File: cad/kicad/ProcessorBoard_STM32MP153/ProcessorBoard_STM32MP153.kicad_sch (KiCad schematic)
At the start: 4 parts

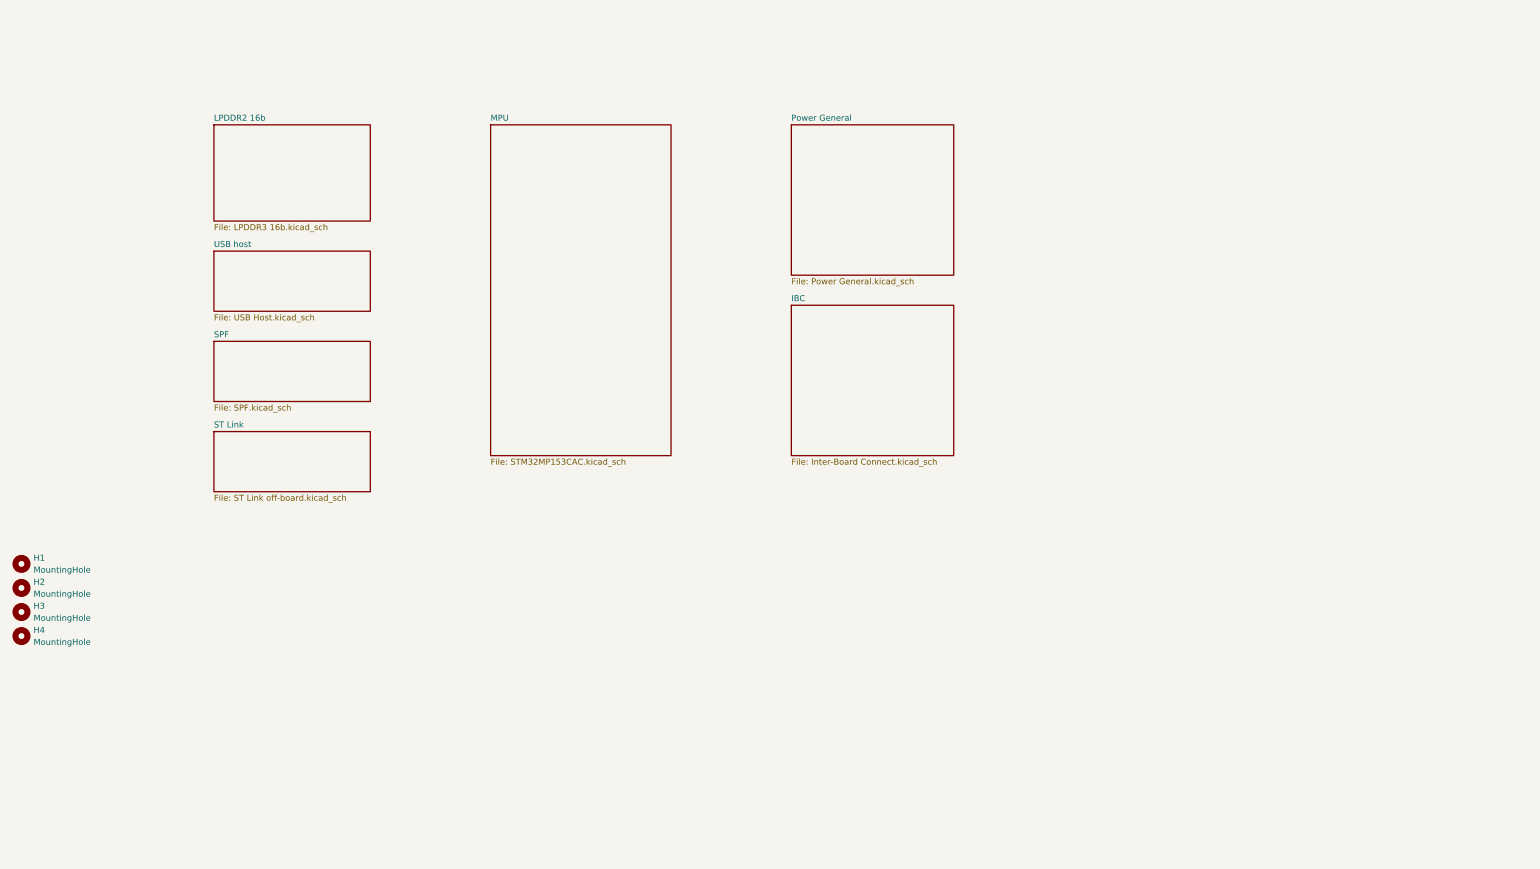
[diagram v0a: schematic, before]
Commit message: piddling with power
11 distinct power nets out :vine_boom:
5V@8A in :vine_boom:
3v3@3A in :vine_boom:
secure os i2c :vine_boom:

:vine_boom:
:vine_boom:
release me
:vine_boom:

these are absolute maximums the PMIC will need, shouldnt get near them unless the outputs shorted. big step up from the dinky 3v3 mcus :(
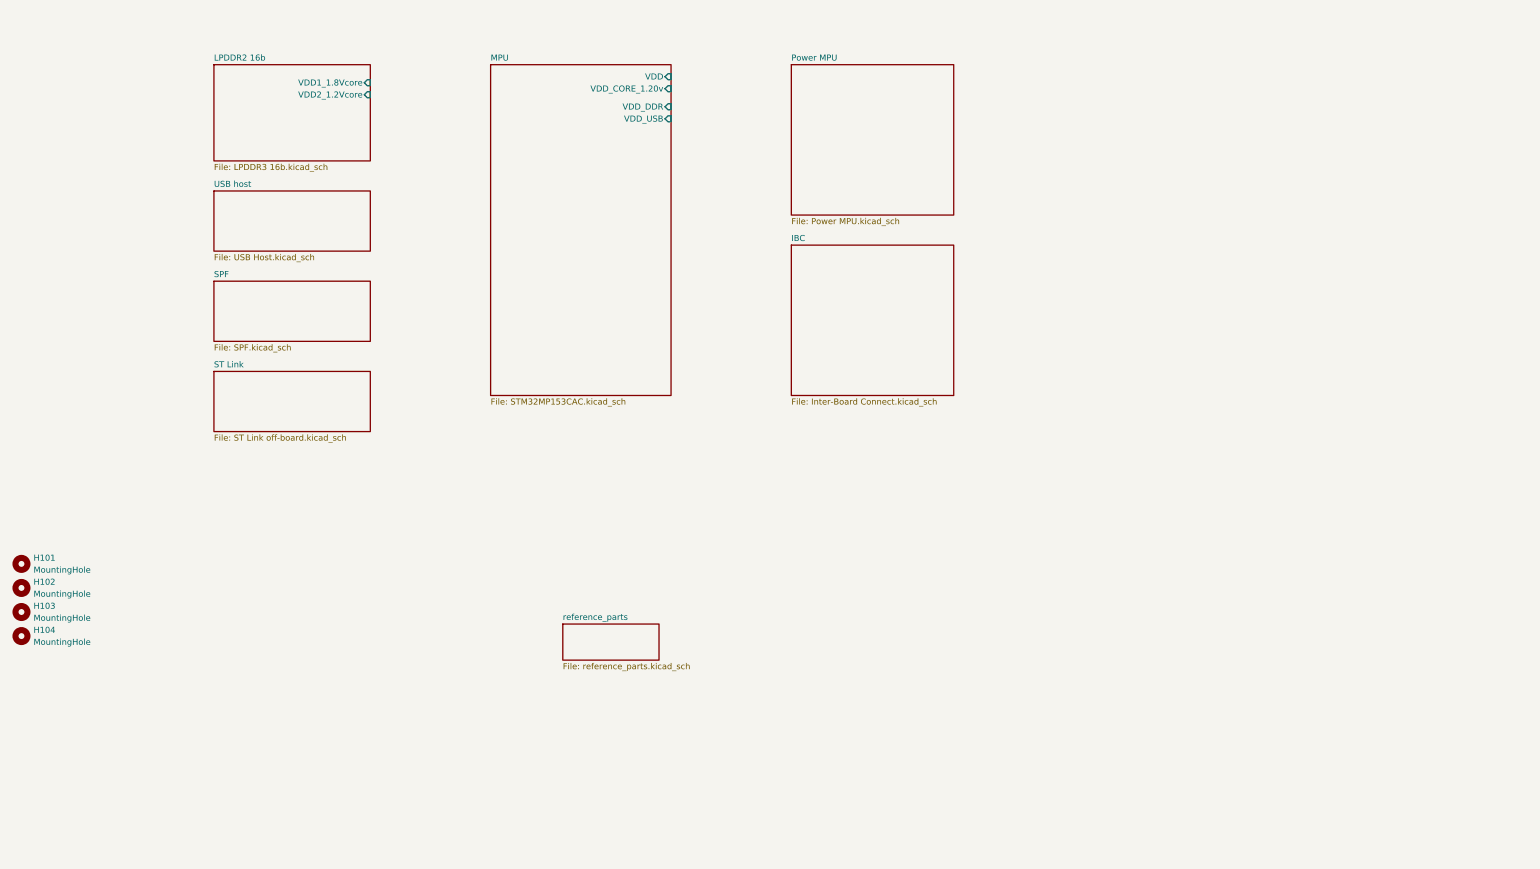
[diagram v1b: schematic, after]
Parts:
- renumbered H1 to H101, H2 to H102, H3 to H103, H4 to H104
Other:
- sheet Power General renamed Power MPU
- added sheet reference_parts (reference_parts.kicad_sch)
- sheet LPDDR2 16b ports: added VDD1_1.8Vcore, VDD2_1.2Vcore; removed none
- sheet MPU ports: added VDD, VDD_CORE_1.20v, VDD_DDR, VDD_USB; removed none
- sheet Power MPU: file Power General.kicad_sch -> Power MPU.kicad_sch
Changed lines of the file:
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@@
 		(dnp no)
 		(fields_autoplaced yes)
-		(property "Reference" "H4"
+		(property "Reference" "H104"
 			(at 30.48 182.8799 0)
 			(show_name no)
@@
 			(project "ProcessorBoard_STM32MP153"
 				(path "/e63e39d7-6ac0-4ffd-8aa3-1841a4541b55"
-					(reference "H4")
+					(reference "H104")
 					(unit 1)
 				)
@@
 		(dnp no)
 		(fields_autoplaced yes)
-		(property "Reference" "H2"
+		(property "Reference" "H102"
 			(at 30.48 172.7199 0)
 			(show_name no)
@@
 			(project "ProcessorBoard_STM32MP153"
 				(path "/e63e39d7-6ac0-4ffd-8aa3-1841a4541b55"
-					(reference "H2")
+					(reference "H102")
 					(unit 1)
 				)
@@
 		(dnp no)
 		(fields_autoplaced yes)
-		(property "Reference" "H3"
+		(property "Reference" "H103"
 			(at 30.48 177.7999 0)
 			(show_name no)
@@
 			(project "ProcessorBoard_STM32MP153"
 				(path "/e63e39d7-6ac0-4ffd-8aa3-1841a4541b55"
-					(reference "H3")
+					(reference "H103")
 					(unit 1)
 				)
@@
 		(dnp no)
 		(fields_autoplaced yes)
-		(property "Reference" "H1"
+		(property "Reference" "H101"
 			(at 30.48 167.6399 0)
 			(show_name no)
@@
 			(project "ProcessorBoard_STM32MP153"
 				(path "/e63e39d7-6ac0-4ffd-8aa3-1841a4541b55"
-					(reference "H1")
+					(reference "H101")
 					(unit 1)
 				)
@@
 	)
 	(sheet
-		(at 190.5 76.2)
+		(at 190.5 63.5)
 		(size 34.29 31.75)
 		(exclude_from_sim no)
@@
 			(color 0 0 0 0)
 		)
-		(property "Sheetname" "Power General"
-			(at 190.5 75.4884 0)
-			(show_name no)
-			(do_not_autoplace no)
-			(effects
-				(font
-					(size 1.27 1.27)
-				)
-				(justify left bottom)
-			)
-		)
-		(property "Sheetfile" "Power General.kicad_sch"
-			(at 190.5 108.5346 0)
+		(property "Sheetname" "Power MPU"
+			(at 190.5 62.7884 0)
+			(show_name no)
+			(do_not_autoplace no)
+			(effects
+				(font
+					(size 1.27 1.27)
+				)
+				(justify left bottom)
+			)
+		)
+		(property "Sheetfile" "Power MPU.kicad_sch"
+			(at 190.5 95.8346 0)
 			(show_name no)
 			(do_not_autoplace no)
@@
 	)
 	(sheet
-		(at 127 76.2)
+		(at 142.24 181.61)
+		(size 20.32 7.62)
+		(exclude_from_sim yes)
+		(in_bom no)
+		(on_board no)
+		(dnp yes)
+		(fields_autoplaced yes)
+		(stroke
+			(width 0.1524)
+			(type solid)
+		)
+		(fill
+			(color 0 0 0 0)
+		)
+		(property "Sheetname" "reference_parts"
+			(at 142.24 180.8984 0)
+			(show_name no)
+			(do_not_autoplace no)
+			(effects
+				(font
+					(size 1.27 1.27)
+				)
+				(justify left bottom)
+			)
+		)
+		(property "Sheetfile" "reference_parts.kicad_sch"
+			(at 142.24 189.8146 0)
+			(show_name no)
+			(do_not_autoplace no)
+			(effects
+				(font
+					(size 1.27 1.27)
+				)
+				(justify left top)
+			)
+		)
+		(instances
+			(project "ProcessorBoard_STM32MP153"
+				(path "/e63e39d7-6ac0-4ffd-8aa3-1841a4541b55"
+					(page "999")
+				)
+			)
+		)
+	)
+	(sheet
+		(at 127 63.5)
 		(size 38.1 69.85)
 		(exclude_from_sim no)
@@
 		)
 		(property "Sheetname" "MPU"
-			(at 127 75.4884 0)
+			(at 127 62.7884 0)
 			(show_name no)
 			(do_not_autoplace no)
@@
 		)
 		(property "Sheetfile" "STM32MP153CAC.kicad_sch"
-			(at 127 146.6346 0)
-			(show_name no)
-			(do_not_autoplace no)
-			(effects
-				(font
-					(size 1.27 1.27)
-				)
-				(justify left top)
+			(at 127 133.9346 0)
+			(show_name no)
+			(do_not_autoplace no)
+			(effects
+				(font
+					(size 1.27 1.27)
+				)
+				(justify left top)
+			)
+		)
+		(pin "VDD" input
+			(at 165.1 66.04 0)
+			(effects
+				(font
+					(size 1.27 1.27)
+				)
+				(justify right)
+			)
+		)
+		(pin "VDD_CORE_1.20v" input
+			(at 165.1 68.58 0)
+			(effects
+				(font
+					(size 1.27 1.27)
+				)
+				(justify right)
+			)
+		)
+		(pin "VDD_DDR" input
+			(at 165.1 72.39 0)
+			(effects
+				(font
+					(size 1.27 1.27)
+				)
+				(justify right)
+			)
+		)
+		(pin "VDD_USB" input
+			(at 165.1 74.93 0)
+			(effects
+				(font
+					(size 1.27 1.27)
+				)
+				(justify right)
 			)
 		)
@@
 	)
 	(sheet
-		(at 68.58 140.97)
+		(at 68.58 128.27)
 		(size 33.02 12.7)
 		(exclude_from_sim no)
@@
 		)
 		(property "Sheetname" "ST Link"
-			(at 68.58 140.2584 0)
+			(at 68.58 127.5584 0)
 			(show_name no)
 			(do_not_autoplace no)
@@
 		)
 		(property "Sheetfile" "ST Link off-board.kicad_sch"
-			(at 68.58 154.2546 0)
+			(at 68.58 141.5546 0)
 			(show_name no)
 			(do_not_autoplace no)
@@
 	)
 	(sheet
-		(at 68.58 121.92)
+		(at 68.58 109.22)
 		(size 33.02 12.7)
 		(exclude_from_sim no)
@@
 		)
 		(property "Sheetname" "SPF"
-			(at 68.58 121.2084 0)
+			(at 68.58 108.5084 0)
 			(show_name no)
 			(do_not_autoplace no)
@@
 		)
 		(property "Sheetfile" "SPF.kicad_sch"
-			(at 68.58 135.2046 0)
+			(at 68.58 122.5046 0)
 			(show_name no)
 			(do_not_autoplace no)
@@
 	)
 	(sheet
-		(at 68.58 102.87)
+		(at 68.58 90.17)
 		(size 33.02 12.7)
 		(exclude_from_sim no)
@@
 		)
 		(property "Sheetname" "USB host"
-			(at 68.58 102.1584 0)
+			(at 68.58 89.4584 0)
 			(show_name no)
 			(do_not_autoplace no)
@@
 		)
 		(property "Sheetfile" "USB Host.kicad_sch"
-			(at 68.58 116.1546 0)
+			(at 68.58 103.4546 0)
 			(show_name no)
 			(do_not_autoplace no)
@@
 	)
 	(sheet
-		(at 190.5 114.3)
+		(at 190.5 101.6)
 		(size 34.29 31.75)
 		(exclude_from_sim no)
@@
 		)
 		(property "Sheetname" "IBC"
-			(at 190.5 113.5884 0)
+			(at 190.5 100.8884 0)
 			(show_name no)
 			(do_not_autoplace no)
@@
 		)
 		(property "Sheetfile" "Inter-Board Connect.kicad_sch"
-			(at 190.5 146.6346 0)
+			(at 190.5 133.9346 0)
 			(show_name no)
 			(do_not_autoplace no)
@@
 	)
 	(sheet
-		(at 68.58 76.2)
+		(at 68.58 63.5)
 		(size 33.02 20.32)
 		(exclude_from_sim no)
@@
 		)
 		(property "Sheetname" "LPDDR2 16b"
-			(at 68.58 75.4884 0)
+			(at 68.58 62.7884 0)
 			(show_name no)
 			(do_not_autoplace no)
@@
 		)
 		(property "Sheetfile" "LPDDR3 16b.kicad_sch"
-			(at 68.58 97.1046 0)
-			(show_name no)
-			(do_not_autoplace no)
-			(effects
-				(font
-					(size 1.27 1.27)
-				)
-				(justify left top)
-			)
-		)
+			(at 68.58 84.4046 0)
+			(show_name no)
+			(do_not_autoplace no)
+			(effects
+				(font
+					(size 1.27 1.27)
+				)
+				(justify left top)
+			)
+		)
+		(pin "VDD1_1.8Vcore" input
+			(at 101.6 67.31 0)
+			(effects
+				(font
+					(size 1.27 1.27)
+				)
+				(justify right)
+			)
+		)
+		(pin "VDD2_1.2Vcore" input
+			(at 101.6 69.85 0)
+			(effects
+				(font
+					(size 1.27 1.27)
+				)
+				(justify right)
+			)
+		)

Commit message: some more caps and power specs
maybe puppy and rainbows if dont use the sw controlled PMIC. ddr dosent seem to care too much about sequencing, and the mpu sequence is 2 steps... but size :( :( :( . wheres muh leaded puckagies :(
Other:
- removed sheet reference_parts
- added sheet reference parts (reference_parts.kicad_sch)
- sheet LPDDR2 16b ports: added none; removed VDD1_1.8Vcore, VDD2_1.2Vcore
- sheet MPU ports: added none; removed VDD, VDD_CORE_1.20v, VDD_DDR, VDD_USB
- sheet Power MPU ports: added GND, PROC_PMIC_IO, PROC_PWR, Vin_prim; removed none
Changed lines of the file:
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@@
 	)
 	(sheet
-		(at 190.5 63.5)
+		(at 190.5 76.2)
 		(size 34.29 31.75)
 		(exclude_from_sim no)
@@
 		)
 		(property "Sheetname" "Power MPU"
-			(at 190.5 62.7884 0)
+			(at 190.5 75.4884 0)
 			(show_name no)
 			(do_not_autoplace no)
@@
 		)
 		(property "Sheetfile" "Power MPU.kicad_sch"
-			(at 190.5 95.8346 0)
-			(show_name no)
-			(do_not_autoplace no)
-			(effects
-				(font
-					(size 1.27 1.27)
-				)
-				(justify left top)
+			(at 190.5 108.5346 0)
+			(show_name no)
+			(do_not_autoplace no)
+			(effects
+				(font
+					(size 1.27 1.27)
+				)
+				(justify left top)
+			)
+		)
+		(pin "GND" input
+			(at 224.79 83.82 0)
+			(effects
+				(font
+					(size 1.27 1.27)
+				)
+				(justify right)
+			)
+		)
+		(pin "PROC_PMIC_IO" bidirectional
+			(at 224.79 86.36 0)
+			(effects
+				(font
+					(size 1.27 1.27)
+				)
+				(justify right)
+			)
+		)
+		(pin "PROC_PWR" output
+			(at 224.79 88.9 0)
+			(effects
+				(font
+					(size 1.27 1.27)
+				)
+				(justify right)
+			)
+		)
+		(pin "Vin_prim" input
+			(at 224.79 91.44 0)
+			(effects
+				(font
+					(size 1.27 1.27)
+				)
+				(justify right)
 			)
 		)
@@
 	)
 	(sheet
-		(at 142.24 181.61)
-		(size 20.32 7.62)
+		(at 309.88 215.9)
+		(size 12.7 12.7)
 		(exclude_from_sim yes)
 		(in_bom no)
@@
 			(color 0 0 0 0)
 		)
-		(property "Sheetname" "reference_parts"
-			(at 142.24 180.8984 0)
+		(property "Sheetname" "reference parts"
+			(at 309.88 215.1884 0)
 			(show_name no)
 			(do_not_autoplace no)
@@
 		)
 		(property "Sheetfile" "reference_parts.kicad_sch"
-			(at 142.24 189.8146 0)
-			(show_name no)
-			(do_not_autoplace no)
-			(effects
-				(font
-					(size 1.27 1.27)
-				)
-				(justify left top)
-			)
-		)
-		(instances
-			(project "ProcessorBoard_STM32MP153"
-				(path "/e63e39d7-6ac0-4ffd-8aa3-1841a4541b55"
-					(page "999")
-				)
-			)
-		)
-	)
-	(sheet
-		(at 127 63.5)
+			(at 309.88 229.1846 0)
+			(show_name no)
+			(do_not_autoplace no)
+			(effects
+				(font
+					(size 1.27 1.27)
+				)
+				(justify left top)
+			)
+		)
+		(instances
+			(project "ProcessorBoard_STM32MP153"
+				(path "/e63e39d7-6ac0-4ffd-8aa3-1841a4541b55"
+					(page "9")
+				)
+			)
+		)
+	)
+	(sheet
+		(at 127 76.2)
 		(size 38.1 69.85)
 		(exclude_from_sim no)
@@
 		)
 		(property "Sheetname" "MPU"
-			(at 127 62.7884 0)
+			(at 127 75.4884 0)
 			(show_name no)
 			(do_not_autoplace no)
@@
 		)
 		(property "Sheetfile" "STM32MP153CAC.kicad_sch"
-			(at 127 133.9346 0)
-			(show_name no)
-			(do_not_autoplace no)
-			(effects
-				(font
-					(size 1.27 1.27)
-				)
-				(justify left top)
-			)
-		)
-		(pin "VDD" input
-			(at 165.1 66.04 0)
-			(effects
-				(font
-					(size 1.27 1.27)
-				)
-				(justify right)
-			)
-		)
-		(pin "VDD_CORE_1.20v" input
-			(at 165.1 68.58 0)
-			(effects
-				(font
-					(size 1.27 1.27)
-				)
-				(justify right)
-			)
-		)
-		(pin "VDD_DDR" input
-			(at 165.1 72.39 0)
-			(effects
-				(font
-					(size 1.27 1.27)
-				)
-				(justify right)
-			)
-		)
-		(pin "VDD_USB" input
-			(at 165.1 74.93 0)
-			(effects
-				(font
-					(size 1.27 1.27)
-				)
-				(justify right)
+			(at 127 146.6346 0)
+			(show_name no)
+			(do_not_autoplace no)
+			(effects
+				(font
+					(size 1.27 1.27)
+				)
+				(justify left top)
 			)
 		)
@@
 	)
 	(sheet
-		(at 68.58 128.27)
+		(at 68.58 140.97)
 		(size 33.02 12.7)
 		(exclude_from_sim no)
@@
 		)
 		(property "Sheetname" "ST Link"
-			(at 68.58 127.5584 0)
+			(at 68.58 140.2584 0)
 			(show_name no)
 			(do_not_autoplace no)
@@
 		)
 		(property "Sheetfile" "ST Link off-board.kicad_sch"
-			(at 68.58 141.5546 0)
+			(at 68.58 154.2546 0)
 			(show_name no)
 			(do_not_autoplace no)
@@
 	)
 	(sheet
-		(at 68.58 109.22)
+		(at 68.58 121.92)
 		(size 33.02 12.7)
 		(exclude_from_sim no)
@@
 		)
 		(property "Sheetname" "SPF"
-			(at 68.58 108.5084 0)
+			(at 68.58 121.2084 0)
 			(show_name no)
 			(do_not_autoplace no)
@@
 		)
 		(property "Sheetfile" "SPF.kicad_sch"
-			(at 68.58 122.5046 0)
+			(at 68.58 135.2046 0)
 			(show_name no)
 			(do_not_autoplace no)
@@
 	)
 	(sheet
-		(at 68.58 90.17)
+		(at 68.58 102.87)
 		(size 33.02 12.7)
 		(exclude_from_sim no)
@@
 		)
 		(property "Sheetname" "USB host"
-			(at 68.58 89.4584 0)
+			(at 68.58 102.1584 0)
 			(show_name no)
 			(do_not_autoplace no)
@@
 		)
 		(property "Sheetfile" "USB Host.kicad_sch"
-			(at 68.58 103.4546 0)
+			(at 68.58 116.1546 0)
 			(show_name no)
 			(do_not_autoplace no)
@@
 	)
 	(sheet
-		(at 190.5 101.6)
+		(at 190.5 114.3)
 		(size 34.29 31.75)
 		(exclude_from_sim no)
@@
 		)
 		(property "Sheetname" "IBC"
-			(at 190.5 100.8884 0)
+			(at 190.5 113.5884 0)
 			(show_name no)
 			(do_not_autoplace no)
@@
 		)
 		(property "Sheetfile" "Inter-Board Connect.kicad_sch"
-			(at 190.5 133.9346 0)
+			(at 190.5 146.6346 0)
 			(show_name no)
 			(do_not_autoplace no)
@@
 	)
 	(sheet
-		(at 68.58 63.5)
+		(at 68.58 76.2)
 		(size 33.02 20.32)
 		(exclude_from_sim no)
@@
 		)
 		(property "Sheetname" "LPDDR2 16b"
-			(at 68.58 62.7884 0)
+			(at 68.58 75.4884 0)
 			(show_name no)
 			(do_not_autoplace no)
@@
 		)
 		(property "Sheetfile" "LPDDR3 16b.kicad_sch"
-			(at 68.58 84.4046 0)
-			(show_name no)
-			(do_not_autoplace no)
-			(effects
-				(font
-					(size 1.27 1.27)
-				)
-				(justify left top)
-			)
-		)
-		(pin "VDD1_1.8Vcore" input
-			(at 101.6 67.31 0)
-			(effects
-				(font
-					(size 1.27 1.27)
-				)
-				(justify right)
-			)
-		)
-		(pin "VDD2_1.2Vcore" input
-			(at 101.6 69.85 0)
-			(effects
-				(font
-					(size 1.27 1.27)
-				)
-				(justify right)
-			)
-		)
+			(at 68.58 97.1046 0)
+			(show_name no)
+			(do_not_autoplace no)
+			(effects
+				(font
+					(size 1.27 1.27)
+				)
+				(justify left top)
+			)
+		)
